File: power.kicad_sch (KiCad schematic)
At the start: 76 parts, among them Q1 BSS138AKA, Q2 SQS401EN-T1_BE3, Q3 BCM857BS-7-F, U3 LMR62014XMF, U4 AP62301_TSOT, U5 AP62301_TSOT, U6 AP22615A_TSOT26

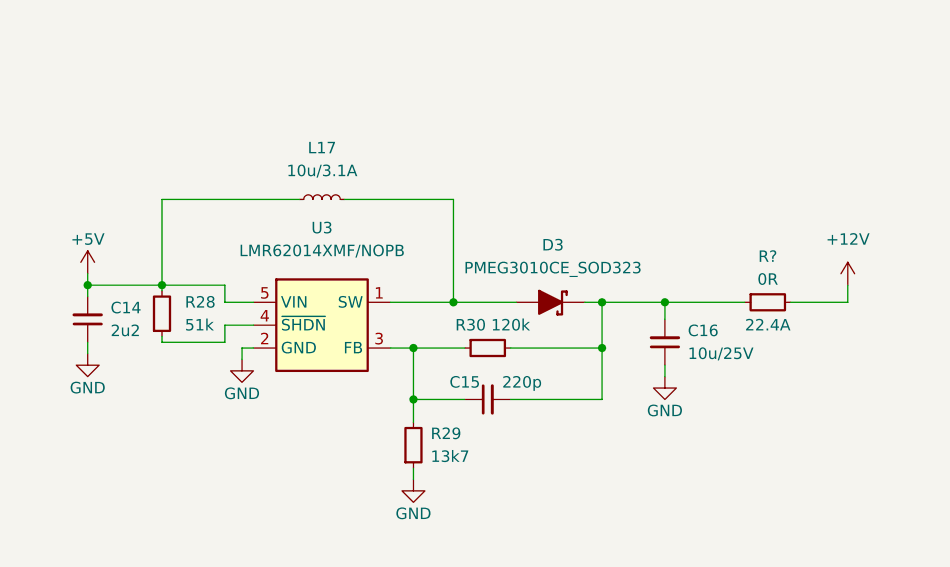
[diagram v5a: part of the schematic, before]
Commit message: Power: add boost converter labels
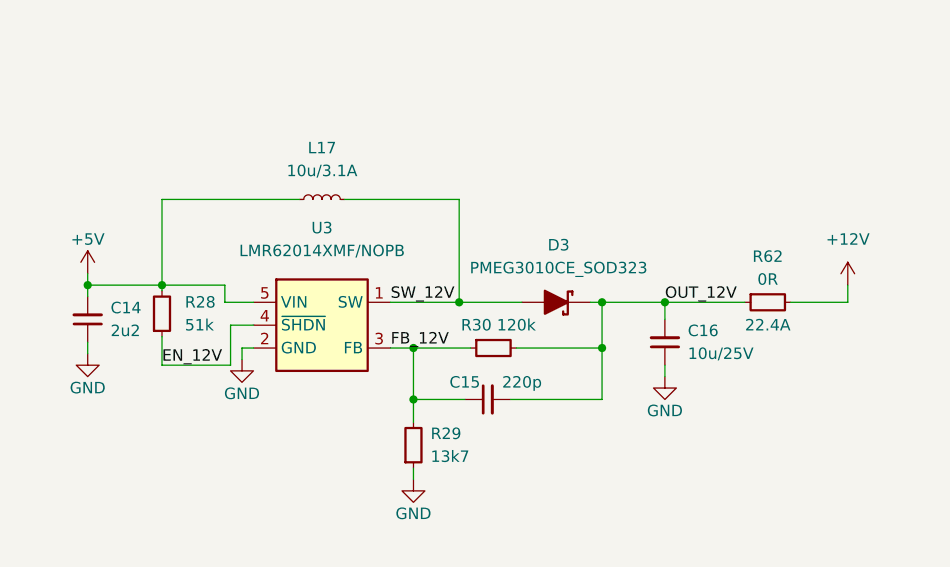
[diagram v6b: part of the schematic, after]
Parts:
- gave numbers to parts that had none: 1
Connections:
- net FB_12V: now reaches C15.1, R29.2, R30.1, U3.3 (FB)
- net OUT_12V: now reaches C15.2, C16.2, D3.K, R30.2, R62.1
- net EN_12V: now reaches R28.1, U3.4 (~{SHDN})
- net SW_12V: now reaches D3.A, L17.2, U3.1 (SW)
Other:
- moved on the sheet: D3, R30
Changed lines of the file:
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@@
   (junction (at 349.25 132.08) (diameter 0) (color 0 0 0 0)
   )
-  (junction (at 220.98 231.775) (diameter 0) (color 0 0 0 0)
-  )
   (junction (at 237.49 236.855) (diameter 0) (color 0 0 0 0)
   )
@@
   (junction (at 114.935 71.755) (diameter 0) (color 0 0 0 0)
   )
+  (junction (at 221.615 231.775) (diameter 0) (color 0 0 0 0)
+  )
   (junction (at 339.725 55.245) (diameter 0) (color 0 0 0 0)
   )
@@
     (stroke (width 0) (type default) (color 0 0 0 0))
   )
-  (wire (pts (xy 227.33 236.855) (xy 237.49 236.855))
+  (wire (pts (xy 227.965 236.855) (xy 237.49 236.855))
     (stroke (width 0) (type default) (color 0 0 0 0))
   )
@@
     (stroke (width 0) (type default) (color 0 0 0 0))
   )
-  (wire (pts (xy 220.98 220.345) (xy 220.98 231.775))
+  (wire (pts (xy 221.615 220.345) (xy 221.615 231.775))
     (stroke (width 0) (type default) (color 0 0 0 0))
   )
@@
     (stroke (width 0) (type default) (color 0 0 0 0))
   )
-  (wire (pts (xy 213.995 231.775) (xy 220.98 231.775))
+  (wire (pts (xy 213.995 231.775) (xy 221.615 231.775))
     (stroke (width 0) (type default) (color 0 0 0 0))
   )
@@
     (stroke (width 0) (type default) (color 0 0 0 0))
   )
-  (wire (pts (xy 216.535 236.855) (xy 222.25 236.855))
+  (wire (pts (xy 216.535 236.855) (xy 222.885 236.855))
     (stroke (width 0) (type default) (color 0 0 0 0))
   )
@@
     (stroke (width 0) (type default) (color 0 0 0 0))
   )
-  (wire (pts (xy 195.58 236.22) (xy 188.595 236.22))
+  (wire (pts (xy 196.215 238.76) (xy 188.595 238.76))
     (stroke (width 0) (type default) (color 0 0 0 0))
   )
@@
     (stroke (width 0) (type default) (color 0 0 0 0))
   )
-  (wire (pts (xy 208.915 220.345) (xy 220.98 220.345))
+  (wire (pts (xy 208.915 220.345) (xy 221.615 220.345))
     (stroke (width 0) (type default) (color 0 0 0 0))
   )
@@
     (stroke (width 0) (type default) (color 0 0 0 0))
   )
-  (wire (pts (xy 188.595 236.22) (xy 188.595 235.585))
+  (wire (pts (xy 188.595 238.76) (xy 188.595 235.585))
     (stroke (width 0) (type default) (color 0 0 0 0))
   )
@@
     (stroke (width 0) (type default) (color 0 0 0 0))
   )
-  (wire (pts (xy 220.98 231.775) (xy 227.965 231.775))
-    (stroke (width 0) (type default) (color 0 0 0 0))
-  )
   (wire (pts (xy 114.935 140.335) (xy 108.585 140.335))
     (stroke (width 0) (type default) (color 0 0 0 0))
   )
-  (wire (pts (xy 195.58 234.315) (xy 195.58 236.22))
+  (wire (pts (xy 196.215 234.315) (xy 196.215 238.76))
     (stroke (width 0) (type default) (color 0 0 0 0))
   )
@@
     (stroke (width 0) (type default) (color 0 0 0 0))
   )
+  (wire (pts (xy 221.615 231.775) (xy 228.6 231.775))
+    (stroke (width 0) (type default) (color 0 0 0 0))
+  )
   (wire (pts (xy 272.415 55.245) (xy 288.29 55.245))
     (stroke (width 0) (type default) (color 0 0 0 0))
@@
     (stroke (width 0) (type default) (color 0 0 0 0))
   )
-  (wire (pts (xy 198.755 234.315) (xy 195.58 234.315))
+  (wire (pts (xy 198.755 234.315) (xy 196.215 234.315))
     (stroke (width 0) (type default) (color 0 0 0 0))
   )
@@
     (stroke (width 0) (type default) (color 0 0 0 0))
   )
-  (wire (pts (xy 237.49 231.775) (xy 235.585 231.775))
+  (wire (pts (xy 237.49 231.775) (xy 236.22 231.775))
     (stroke (width 0) (type default) (color 0 0 0 0))
   )
@@
     (effects (font (size 1.27 1.27)) (justify left bottom))
   )
+  (label "EN_12V" (at 188.595 238.76 0)
+    (effects (font (size 1.27 1.27)) (justify left bottom))
+  )
+  (label "OUT_12V" (at 244.475 231.775 0)
+    (effects (font (size 1.27 1.27)) (justify left bottom))
+  )
   (label "EN_1V8" (at 280.67 60.325 0)
     (effects (font (size 1.27 1.27)) (justify left bottom))
@@
     (effects (font (size 1.27 1.27)) (justify left bottom))
   )
+  (label "SW_12V" (at 213.995 231.775 0)
+    (effects (font (size 1.27 1.27)) (justify left bottom))
+  )
+  (label "FB_12V" (at 213.995 236.855 0)
+    (effects (font (size 1.27 1.27)) (justify left bottom))
+  )
   (label "OUT_1V2" (at 340.36 132.08 0)
     (effects (font (size 1.27 1.27)) (justify left bottom))
@@
     (pin "2")
   )
-  (symbol (lib_id "antmicroResistors0402:R_120k_0402") (at 222.25 236.855 0) (unit 1)
+  (symbol (lib_id "antmicroResistors0402:R_120k_0402") (at 222.885 236.855 0) (unit 1)
     (in_bom yes) (on_board yes)
-    (property "Reference" "R30" (id 0) (at 222.885 234.315 0)
+    (property "Reference" "R30" (id 0) (at 223.52 234.315 0)
       (effects (font (size 1.27 1.27) (thickness 0.15)))
     )
-    (property "Value" "R_120k_0402" (id 1) (at 242.57 249.555 0)
+    (property "Value" "R_120k_0402" (id 1) (at 243.205 249.555 0)
       (effects (font (size 1.27 1.27) (thickness 0.15)) (justify left bottom) hide)
     )
-    (property "Footprint" "antmicro-footprints:R_0402_1005Metric" (id 2) (at 242.57 252.095 0)
+    (property "Footprint" "antmicro-footprints:R_0402_1005Metric" (id 2) (at 243.205 252.095 0)
       (effects (font (size 1.27 1.27) (thickness 0.15)) (justify left bottom) hide)
     )
-    (property "Datasheet" "https://www.bourns.com/docs/product-datasheets/cr.pdf" (id 3) (at 242.57 254.635 0)
+    (property "Datasheet" "https://www.bourns.com/docs/product-datasheets/cr.pdf" (id 3) (at 243.205 254.635 0)
       (effects (font (size 1.27 1.27) (thickness 0.15)) (justify left bottom) hide)
     )
-    (property "MPN" "CR0402-FX-1203GLF" (id 4) (at 242.57 257.175 0)
+    (property "MPN" "CR0402-FX-1203GLF" (id 4) (at 243.205 257.175 0)
       (effects (font (size 1.27 1.27) (thickness 0.15)) (justify left bottom) hide)
     )
-    (property "Manufacturer" "Bourns" (id 5) (at 242.57 259.715 0)
+    (property "Manufacturer" "Bourns" (id 5) (at 243.205 259.715 0)
       (effects (font (size 1.27 1.27) (thickness 0.15)) (justify left bottom) hide)
     )
-    (property "License" "Apache-2.0" (id 6) (at 242.57 262.255 0)
+    (property "License" "Apache-2.0" (id 6) (at 243.205 262.255 0)
       (effects (font (size 1.27 1.27) (thickness 0.15)) (justify left bottom) hide)
     )
-    (property "Author" "Antmicro" (id 7) (at 242.57 264.795 0)
+    (property "Author" "Antmicro" (id 7) (at 243.205 264.795 0)
       (effects (font (size 1.27 1.27) (thickness 0.15)) (justify left bottom) hide)
     )
-    (property "Val" "120k" (id 8) (at 227.33 234.315 0)
+    (property "Val" "120k" (id 8) (at 227.965 234.315 0)
       (effects (font (size 1.27 1.27) (thickness 0.15)))
     )
-    (property "Tolerance" "1%" (id 9) (at 242.57 247.015 0)
+    (property "Tolerance" "1%" (id 9) (at 243.205 247.015 0)
       (effects (font (size 1.27 1.27)) (justify left bottom) hide)
     )
@@
     (pin "2")
   )
-  (symbol (lib_id "antmicroDiodesRectifiersSingle:PMEG3010CE_SOD323") (at 227.965 231.775 0) (unit 1)
+  (symbol (lib_id "antmicroDiodesRectifiersSingle:PMEG3010CE_SOD323") (at 228.6 231.775 0) (unit 1)
     (in_bom yes) (on_board yes) (fields_autoplaced)
-    (property "Reference" "D3" (id 0) (at 232.029 225.425 0)
+    (property "Reference" "D3" (id 0) (at 232.664 225.425 0)
       (effects (font (size 1.27 1.27) (thickness 0.15)))
     )
-    (property "Value" "PMEG3010CE_SOD323" (id 1) (at 232.029 227.965 0)
+    (property "Value" "PMEG3010CE_SOD323" (id 1) (at 232.664 227.965 0)
       (effects (font (size 1.27 1.27) (thickness 0.15)))
     )
-    (property "Footprint" "antmicro-footprints:D_SOD-323F" (id 2) (at 250.825 241.935 0)
+    (property "Footprint" "antmicro-footprints:D_SOD-323F" (id 2) (at 251.46 241.935 0)
       (effects (font (size 1.27 1.27) (thickness 0.15)) (justify left bottom) hide)
     )
-    (property "Datasheet" "https://assets.nexperia.com/documents/data-sheet/PMEG3010CEH_PMEG3010CEJ.pdf" (id 3) (at 250.825 244.475 0)
+    (property "Datasheet" "https://assets.nexperia.com/documents/data-sheet/PMEG3010CEH_PMEG3010CEJ.pdf" (id 3) (at 251.46 244.475 0)
       (effects (font (size 1.27 1.27) (thickness 0.15)) (justify left bottom) hide)
     )
-    (property "MPN" "PMEG3010CEJ" (id 4) (at 250.825 247.015 0)
+    (property "MPN" "PMEG3010CEJ" (id 4) (at 251.46 247.015 0)
       (effects (font (size 1.27 1.27) (thickness 0.15)) (justify left bottom) hide)
     )
-    (property "Manufacturer" "Nexperia" (id 5) (at 250.825 249.555 0)
+    (property "Manufacturer" "Nexperia" (id 5) (at 251.46 249.555 0)
       (effects (font (size 1.27 1.27) (thickness 0.15)) (justify left bottom) hide)
     )
-    (property "Author" "Antmicro" (id 6) (at 250.825 252.095 0)
+    (property "Author" "Antmicro" (id 6) (at 251.46 252.095 0)
       (effects (font (size 1.27 1.27) (thickness 0.15)) (justify left bottom) hide)
     )
-    (property "License" "Apache-2.0" (id 7) (at 250.825 254.635 0)
+    (property "License" "Apache-2.0" (id 7) (at 251.46 254.635 0)
       (effects (font (size 1.27 1.27) (thickness 0.15)) (justify left bottom) hide)
     )
@@
   (symbol (lib_id "antmicroResistors0603:R_0R_22.4A_0603") (at 253.365 231.775 0) (unit 1)
     (in_bom yes) (on_board yes)
-    (property "Reference" "R?" (id 0) (at 255.905 226.695 0)
+    (property "Reference" "R62" (id 0) (at 255.905 226.695 0)
       (effects (font (size 1.27 1.27) (thickness 0.15)))
     )

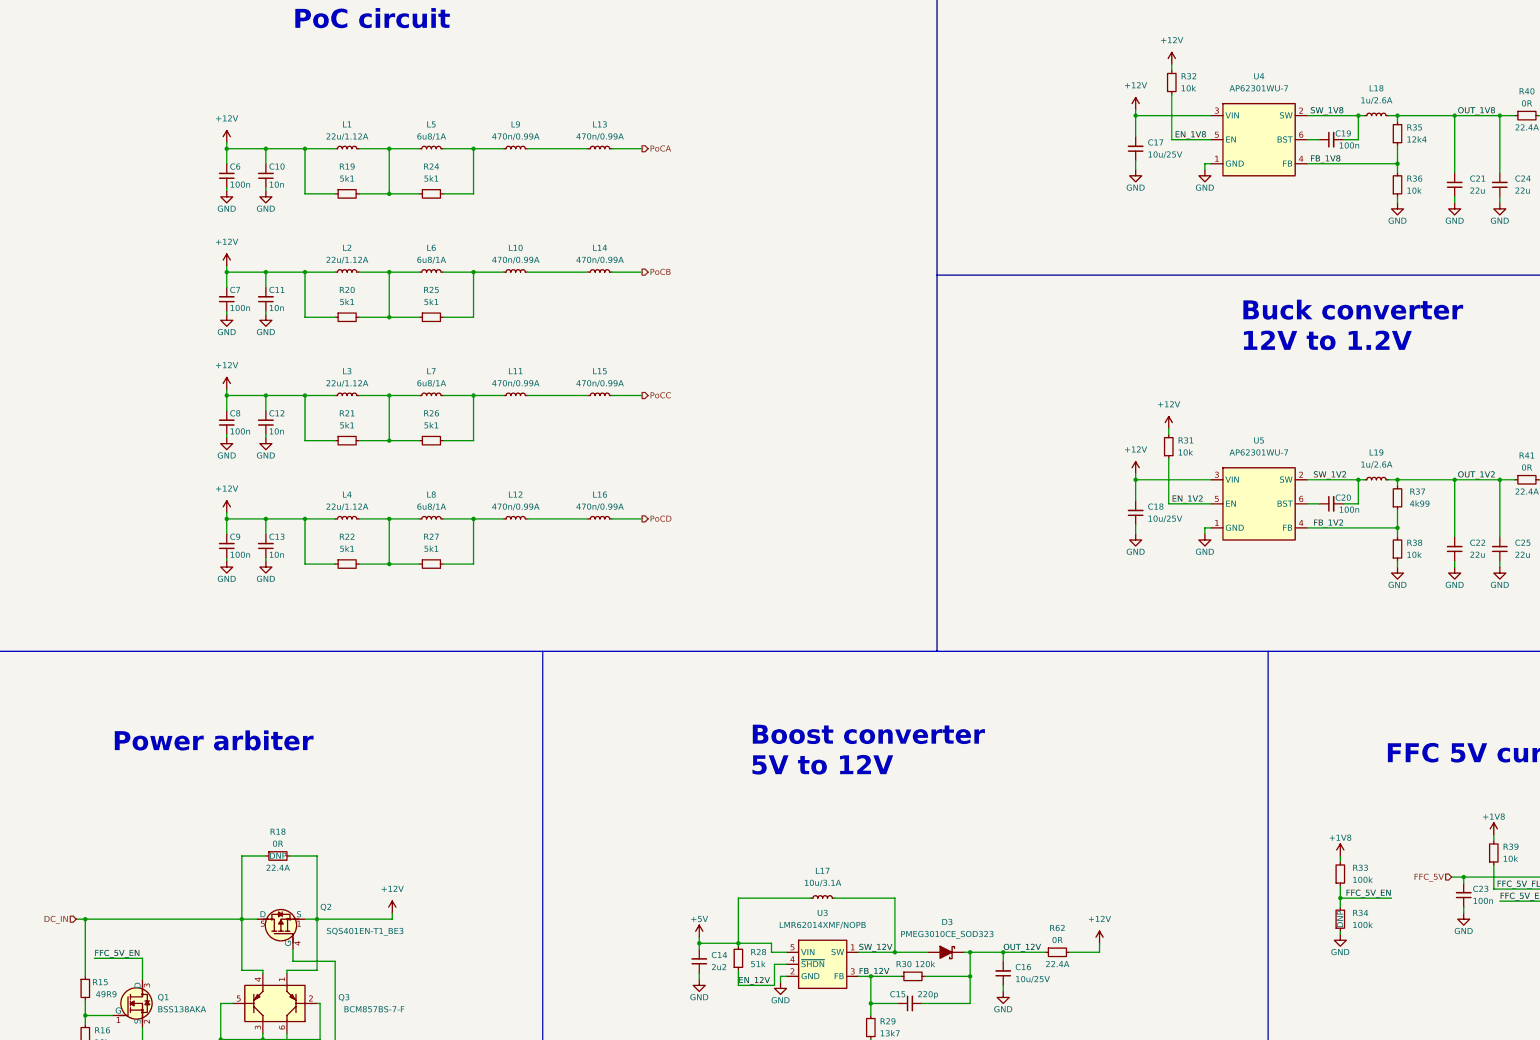
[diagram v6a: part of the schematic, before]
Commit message: Connectors: replace i2c buffer gate with proper level shifter, Power: add test points
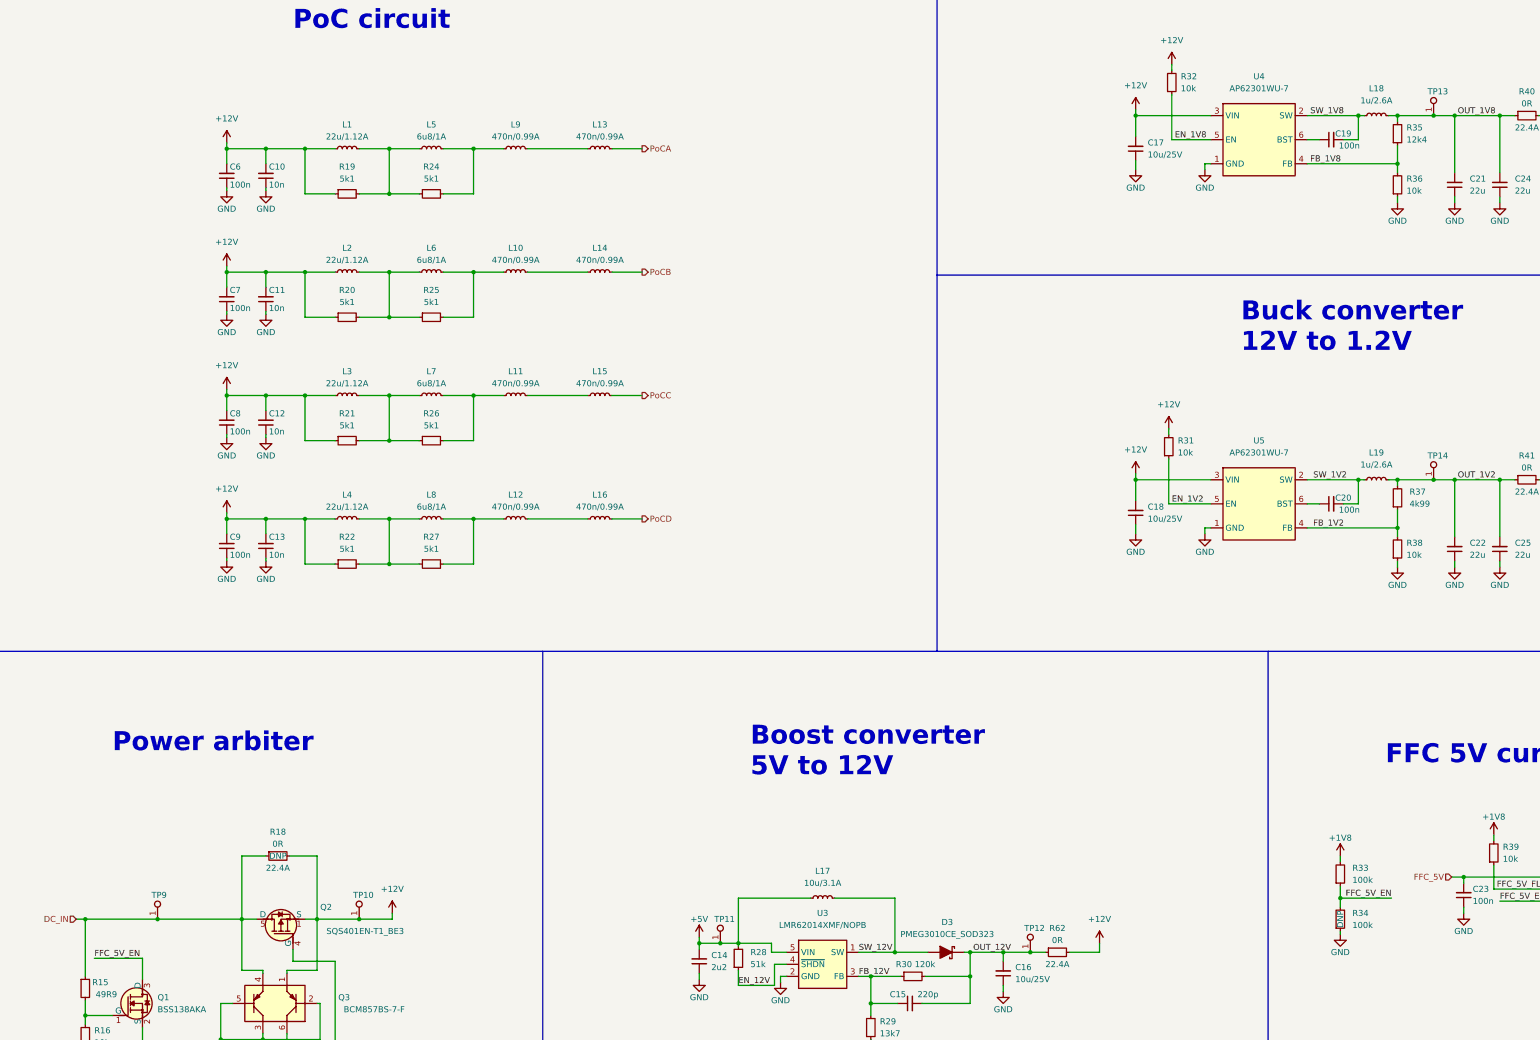
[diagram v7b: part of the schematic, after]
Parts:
- added TP10, TP11, TP12, TP13, TP14, TP9: TP_0.75mm_SMD, antmicro-footprints:TP_SMD_0.75mm, symbol antmicroTestPoints:TP_0.75mm_SMD
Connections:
- net +12V: now also TP10.1
- net +5V: now also TP11.1
- net DC_IN: now also TP9.1
- net OUT_12V: now also TP12.1
- net OUT_1V2: now also TP14.1
- net OUT_1V8: now also TP13.1

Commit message: Update diagram
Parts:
- added TP15: TP_0.75mm_SMD, antmicro-footprints:TP_SMD_0.75mm, symbol antmicroTestPoints:TP_0.75mm_SMD
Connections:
- net GND: now also TP15.1
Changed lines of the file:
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@@
     (pin "2")
+  )
+  (symbol (lib_id "antmicroTestPoints:TP_0.75mm_SMD") (at 62.865 253.365 0) (unit 1)
+    (in_bom yes) (on_board yes)
+    (property "Reference" "TP15" (id 0) (at 67.945 252.095 90)
+      (effects (font (size 1.27 1.27) (thickness 0.15)) (justify right))
+    )
+    (property "Value" "TP_0.75mm_SMD" (id 1) (at 73.66 257.175 0)
+      (effects (font (size 1.27 1.27) (thickness 0.15)) (justify left bottom) hide)
+    )
+    (property "Footprint" "antmicro-footprints:TP_SMD_0.75mm" (id 2) (at 73.66 259.715 0)
+      (effects (font (size 1.27 1.27) (thickness 0.15)) (justify left bottom) hide)
+    )
+    (property "Datasheet" "" (id 3) (at 80.645 266.065 0)
+      (effects (font (size 1.27 1.27) (thickness 0.15)) (justify left bottom) hide)
+    )
+    (property "MPN" "" (id 4) (at 73.66 264.795 0)
+      (effects (font (size 1.27 1.27) (thickness 0.15)) (justify left bottom) hide)
+    )
+    (property "Manufacturer" "" (id 5) (at 73.66 259.715 0)
+      (effects (font (size 1.27 1.27) (thickness 0.15)) (justify left bottom) hide)
+    )
+    (property "Author" "Antmicro" (id 6) (at 73.66 262.255 0)
+      (effects (font (size 1.27 1.27) (thickness 0.15)) (justify left bottom) hide)
+    )
+    (property "License" "Apache-2.0" (id 7) (at 73.66 264.795 0)
+      (effects (font (size 1.27 1.27) (thickness 0.15)) (justify left bottom) hide)
+    )
+    (pin "1")
   )
   (symbol (lib_id "antmicroResistors0402:R_49R9_0402") (at 50.8 236.855 90) (mirror x) (unit 1)
